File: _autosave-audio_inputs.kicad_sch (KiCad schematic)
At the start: 6 parts, among them J2 PLR237/T10BK, U5 DIR9001PW

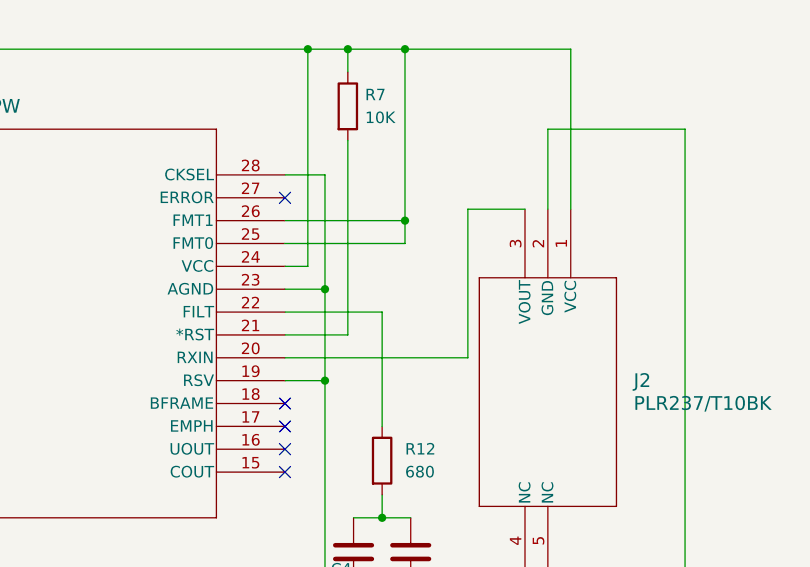
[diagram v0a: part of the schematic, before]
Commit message: Fixed problems with zone fills and general PCB hell
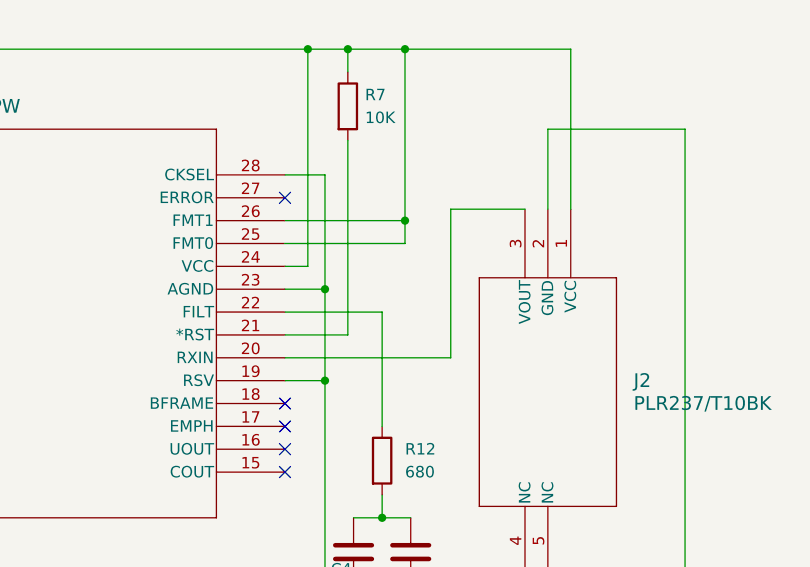
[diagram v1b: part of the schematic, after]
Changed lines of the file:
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@@
 	(wire
 		(pts
-			(xy 158.75 115.57) (xy 158.75 99.06)
+			(xy 156.845 115.57) (xy 156.845 99.06)
 		)
 		(stroke
@@
 	(wire
 		(pts
-			(xy 138.43 115.57) (xy 158.75 115.57)
+			(xy 138.43 115.57) (xy 156.845 115.57)
 		)
 		(stroke
@@
 	(wire
 		(pts
-			(xy 158.75 99.06) (xy 165.1 99.06)
+			(xy 156.845 99.06) (xy 165.1 99.06)
 		)
 		(stroke
